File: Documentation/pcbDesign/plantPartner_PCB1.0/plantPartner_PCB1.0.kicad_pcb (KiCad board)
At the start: 2 copper layers, 148.3 x 67.3 mm, 86 parts, among them IC1 MPM3610, J1 Conn_01x04, J10 Screw_Terminal_01x03, J11 Conn_01x02, J12 Conn_01x03, J13 Conn_01x03, J14 Conn_01x03, J15 Conn_01x03, J16 Conn_01x04, J17 Conn_01x03, J18 Screw_Terminal_01x02, J19 Barrel_Jack, J2 Conn_01x04, J20 Conn_02x04_Top_Bottom, J21 Conn_01x04, J22 Conn_01x04, J23 Conn_01x01, J24 Conn_01x03, J25 Conn_01x03, J26 Conn_01x01, J27 Conn_01x01, J28 Conn_01x01, J29 Conn_01x02, J3 Conn_01x04, J30 Screw_Terminal_01x02, J4 Screw_Terminal, J5 Conn_01x02, J6 Screw_Terminal_01x03, J7 Conn_01x03, J8 Conn_02x04_Top_Bottom, J9 Conn_01x03, K1 SRD-05VDC-SL-C, K2 SRD-05VDC-SL-C, Q1 PNP, Q2 PNP, Q4 AO3400A, U1 EL357N-G, U2 MAX485, U3 ESP32-DEVKIT-V1, U4 EL357N-G

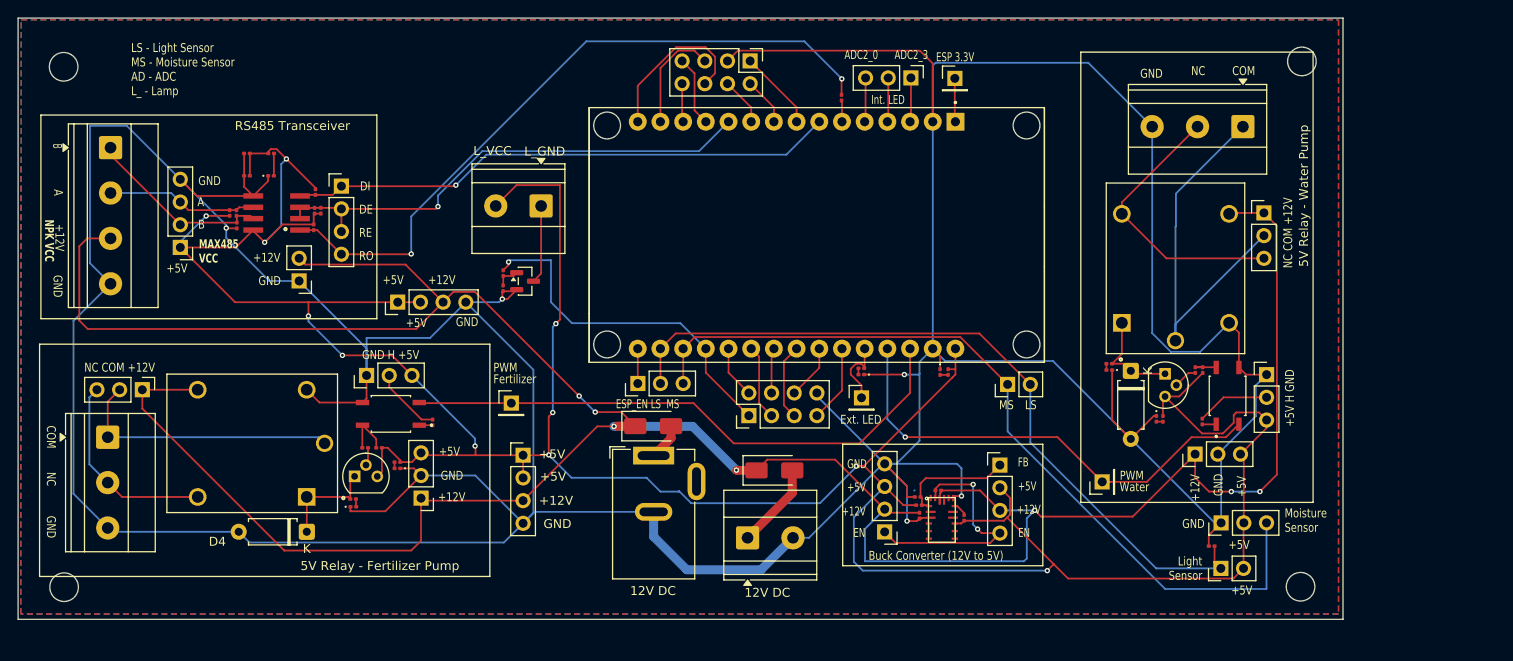
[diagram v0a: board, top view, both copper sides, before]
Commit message: Made some adjustments to PCB to fit JLCPCB standards. When going to order PCB realized I needed LCSC values. I spent the rest of the time trying to setup the JLCPCB tools plugin with zero success.
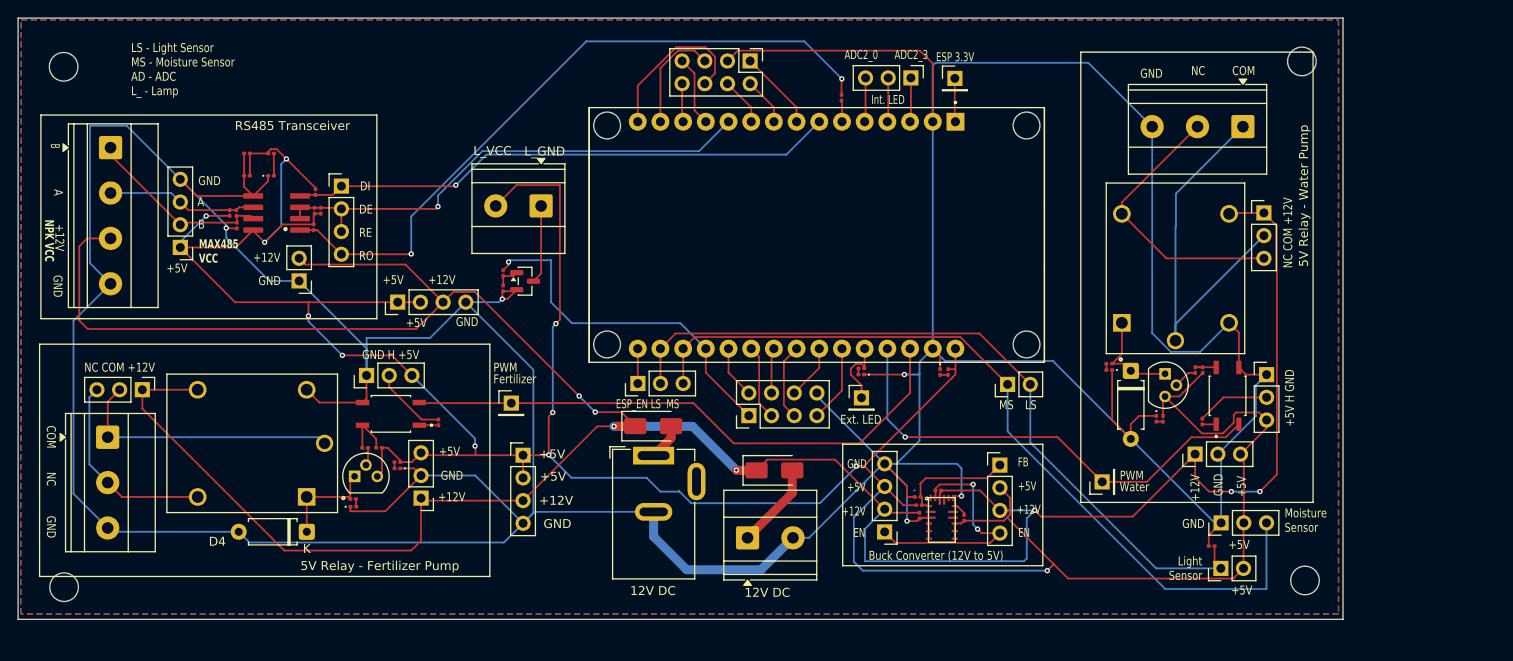
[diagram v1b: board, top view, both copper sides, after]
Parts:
- moved BottomRight 0.86 mm to (207.2, 114.2)
- moved R13 0.64 mm to (110.2, 96.6)
- renumbered REF** to BottomLeft, REF** to BottomRight, REF** to TopLeft, REF** to TopRight
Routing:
- net GND: track 579.2 -> 580.2 mm
- net Net-(R13-Pad2): track 1.54 -> 2.19 mm
- net /H: track 15.9 -> 16.5 mm
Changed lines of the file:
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@@
 		(tenting front back)
 		(pcbplotparams
-			(layerselection 0x00000000_00000000_55555555_575575ff)
+			(layerselection 0x00000000_00000000_55555555_5755f5ff)
 			(plot_on_all_layers_selection 0x00000000_00000000_00000000_00000000)
 			(disableapertmacros no)
@@
 			(usegerberattributes yes)
 			(usegerberadvancedattributes yes)
-			(creategerberjobfile yes)
+			(creategerberjobfile no)
 			(dashed_line_dash_ratio 12.000000)
 			(dashed_line_gap_ratio 3.000000)
@@
 			(sketchdnponfab yes)
 			(crossoutdnponfab yes)
-			(subtractmaskfromsilk yes)
+			(subtractmaskfromsilk no)
 			(outputformat 1)
 			(mirror no)
 			(drillshape 0)
 			(scaleselection 1)
-			(outputdirectory "")
+			(outputdirectory "GerberDrillFiles/")
 		)
 	)
@@
 	(footprint "Resistor_SMD:R_0201_0603Metric"
 		(layer "F.Cu")
-		(at 109.605 96.555 -90)
+		(at 110.25 96.555 -90)
 		(descr "Resistor SMD 0201 (0603 Metric), square (rectangular) end terminal, IPC-7351 nominal, (Body size source: https://www.vishay.com/docs/20052/crcw0201e3.pdf), generated with kicad-footprint-generator")
 		(tags "resistor")
@@
 		(descr "Mounting Hole 3.2mm, M3, no annular, generated by kicad-footprint-generator mountinghole.py")
 		(tags "mountinghole M3")
-		(property "Reference" "REF**"
+		(property "Reference" "TopLeft"
 			(at 0 -4.15 0)
 			(layer "F.SilkS")
@@
 		(descr "Mounting Hole 3.2mm, M3, no annular, generated by kicad-footprint-generator mountinghole.py")
 		(tags "mountinghole M3")
-		(property "Reference" "REF**"
+		(property "Reference" "TopRight"
 			(at 0 -4.15 0)
 			(layer "F.SilkS")
@@
 		(descr "Mounting Hole 3.2mm, M3, no annular, generated by kicad-footprint-generator mountinghole.py")
 		(tags "mountinghole M3")
-		(property "Reference" "REF**"
+		(property "Reference" "BottomLeft"
 			(at 0 -4.15 0)
 			(layer "F.SilkS")
@@
 		(tags "resistor")
 		(property "Reference" "R10"
-			(at 1.765 -0.2388 90)
+			(at 1.765 -0.6388 90)
 			(layer "B.SilkS")
 			(effects
@@
 	(footprint "MountingHole:MountingHole_3.2mm_M3"
 		(layer "F.Cu")
-		(at 206.75 114.95)
+		(at 207.25 114.25)
 		(descr "Mounting Hole 3.2mm, M3, no annular, generated by kicad-footprint-generator mountinghole.py")
 		(tags "mountinghole M3")
-		(property "Reference" "REF**"
+		(property "Reference" "BottomRight"
 			(at 0 -4.15 0)
 			(layer "F.SilkS")
@@
 		(fp_text user "K"
 			(at 0 -1.9 90)
-			(layer "F.SilkS")
-			(effects
-				(font
-					(size 1 1)
-					(thickness 0.15)
-				)
-			)
-		)
-		(fp_text user "K"
-			(at 0 -1.9 90)
 			(layer "F.Fab")
 			(effects
@@
 	)
 	(gr_text "B"
-		(at 67 65.35 270)
+		(at 66.75 65.35 270)
 		(layer "F.SilkS")
 		(effects
@@
 	)
 	(segment
+		(start 188.67 95.83)
+		(end 187.75 96.75)
+		(width 0.2)
+		(layer "F.Cu")
+		(net 1)
+	)
+	(segment
 		(start 81.355 69.35)
 		(end 83.215 71.21)
@@
 	)
 	(segment
-		(start 190.324999 95.83)
-		(end 187.75 98.404999)
-		(width 0.2)
-		(layer "F.Cu")
-		(net 1)
-	)
-	(segment
 		(start 87.47 108.375)
 		(end 87.895 108.8)
@@
 	)
 	(segment
-		(start 83.215 71.21)
-		(end 89.5226 71.21)
+		(start 187.75 96.75)
+		(end 187.75 98.404999)
 		(width 0.2)
 		(layer "F.Cu")
@@
 	(segment
 		(start 190.61 95.83)
-		(end 190.324999 95.83)
+		(end 188.67 95.83)
+		(width 0.2)
+		(layer "F.Cu")
+		(net 1)
+	)
+	(segment
+		(start 83.215 71.21)
+		(end 89.5226 71.21)
 		(width 0.2)
 		(layer "F.Cu")
@@
 	)
 	(segment
+		(start 110.25 96.875)
+		(end 109.605 96.875)
+		(width 0.2)
+		(layer "F.Cu")
+		(net 10)
+	)
+	(segment
 		(start 108.138 96.9)
 		(end 108.108 96.87)
@@
 	)
 	(segment
-		(start 104.745 91.3)
+		(start 108.361 96.235)
 		(end 104.745 92.619)
 		(width 0.2)
@@
 	)
 	(segment
-		(start 108.361 96.235)
-		(end 109.605 96.235)
+		(start 198.135 93.75)
+		(end 195.75 96.135)
 		(width 0.2)
 		(layer "F.Cu")
@@
 	)
 	(segment
-		(start 198.135 93.75)
-		(end 195.75 96.135)
+		(start 202.95 93.75)
+		(end 198.135 93.75)
 		(width 0.2)
 		(layer "F.Cu")
@@
 	(segment
 		(start 104.745 92.619)
-		(end 108.361 96.235)
+		(end 104.745 91.3)
 		(width 0.2)
 		(layer "F.Cu")
@@
 	)
 	(segment
-		(start 202.95 93.75)
-		(end 198.135 93.75)
+		(start 110.25 96.235)
+		(end 108.361 96.235)
 		(width 0.2)
 		(layer "F.Cu")

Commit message: I got the plugin finally working! I had some messed up Python modules that I had to remove and then reinstall. I have also now learned that the footprints I chose for the PCB were too small and classified as extended for JLCPCB which means more 4189. So now I have to change all the Resistor, Capacitor, and Diode footprints to a bigger size to not cost too much. This will then also result in me having to route these small parts again. I am tired of my lack of PCB design knowledge but I think I might be done after this.
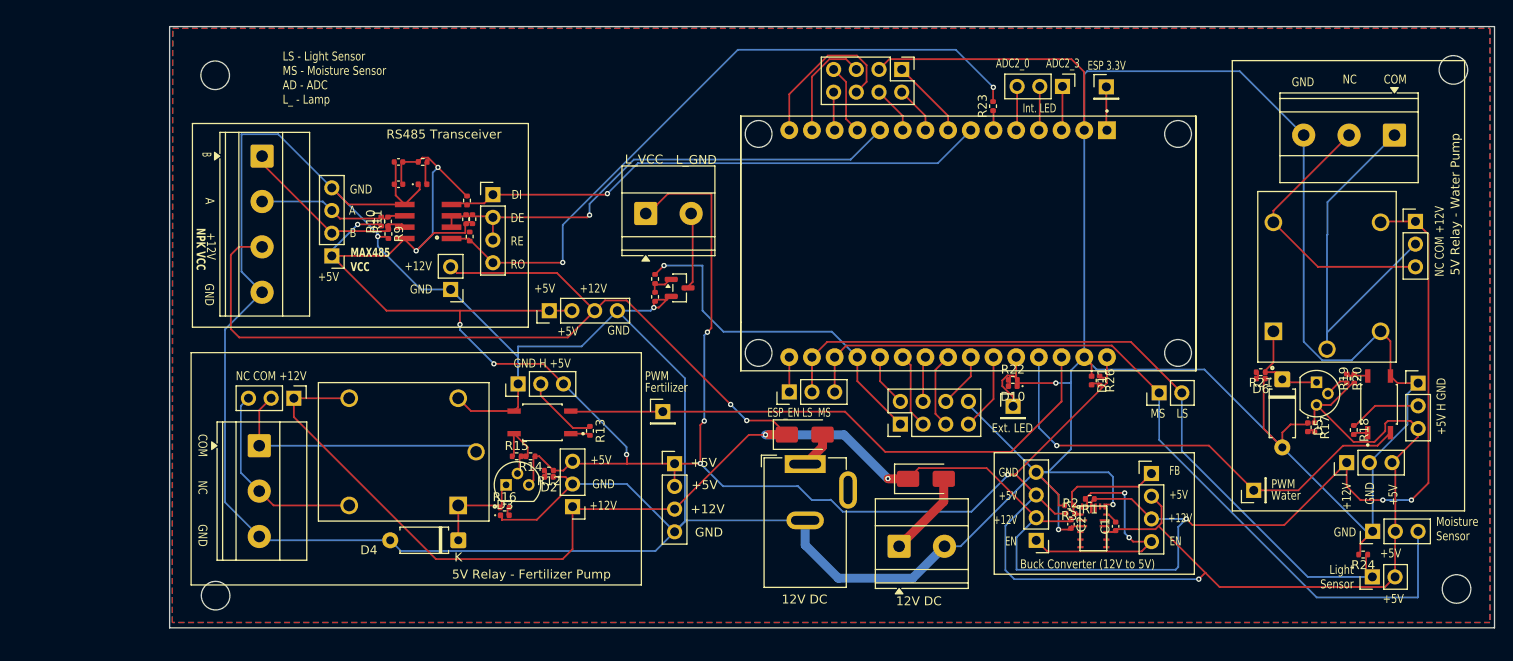
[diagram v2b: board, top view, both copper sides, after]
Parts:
- C1, C2, C3, C4: footprint Capacitor_SMD:C_0201_0603Metric -> Capacitor_SMD:C_0402_1005Metric
- D1, D10, D11, D2, D3, D5, D6: footprint LED_SMD:LED_0201_0603Metric -> LED_SMD:LED_0402_1005Metric
- R1, R10, R11, R12, R13, R14, R15, R16, R17, R18, R19, R2, R20, R21, R22, R23, R24, R25, R26, R27, R3, R4, R5, R6, R7, R8, R9: footprint Resistor_SMD:R_0201_0603Metric -> Resistor_SMD:R_0402_1005Metric
- moved R4 17.5 mm to (113.8, 75.8)
- moved Q4 17.3 mm to (137.2, 81.5)
- moved R27 17.0 mm to (134.5, 82.5)
- moved R25 17.0 mm to (134.5, 80.5)
- moved D10 17.0 mm to (174.5, 92.5)
- moved R22 17.0 mm to (174.5, 91.8)
- moved BottomLeft 17.0 mm to (85.3, 116.0)
- moved BottomRight 17.0 mm to (224.2, 115.2)
- moved C1 17.0 mm to (186.1, 108.2)
- moved C2 17.0 mm to (181.1, 107.9)
- moved C3 17.0 mm to (105.8, 69.9)
- moved C4 17.0 mm to (105.8, 67.4)
- moved D11 17.0 mm to (183.4, 91.9)
- moved D2 17.0 mm to (122.6, 102.7)
- moved D3 17.0 mm to (117.7, 107.0)
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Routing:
- net +5V: track 352.4 -> 361.1 mm
- net /Drain: track 8.78 -> 0.00 mm

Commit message: Rerouted the resistors, capacitors, and LEDs. Surely I can now generate the Drill & Gerber files for printing with no issues
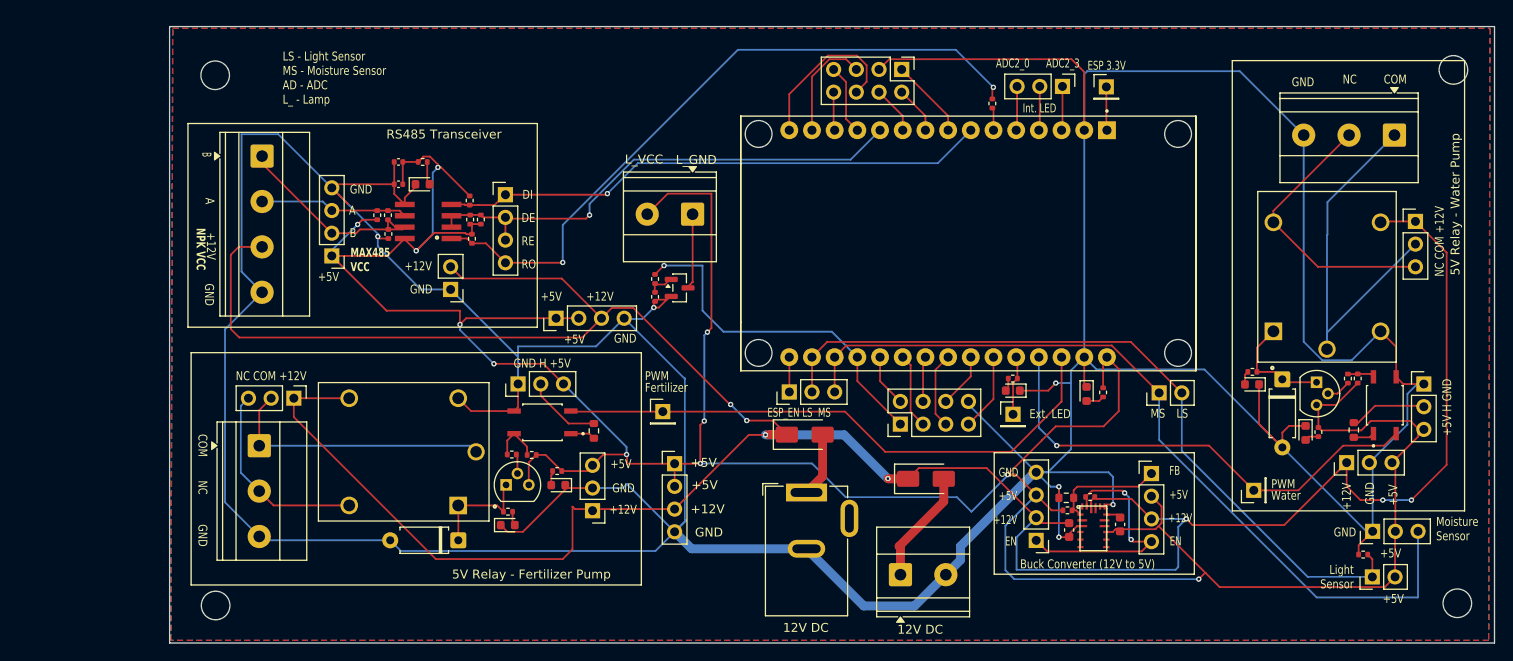
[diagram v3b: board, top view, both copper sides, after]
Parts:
- C1, C2: footprint Capacitor_SMD:C_0402_1005Metric -> Capacitor_SMD:C_0603_1608Metric
- D1, D10, D11, D2, D3, D5, D6: footprint LED_SMD:LED_0402_1005Metric -> LED_SMD:LED_0603_1608Metric
- R13, R18, R3: footprint Resistor_SMD:R_0402_1005Metric -> Resistor_SMD:R_0603_1608Metric
- moved J30 5.25 mm to (138.7, 73.2), turned to 180 degrees
- moved J19 3.18 mm to (151.4, 104.4)
- moved J18 3.18 mm to (162.0, 113.6)
- moved J14 2.28 mm to (127.5, 106.4)
- moved D11 1.60 mm to (182.8, 93.4)
- moved BottomRight 1.60 mm to (224.3, 116.8)
- moved J2 1.40 mm to (117.8, 71.1)
- moved D2 1.40 mm to (123.7, 103.6)
- moved R26 1.39 mm to (184.7, 93.2)
- moved D6 1.18 mm to (201.3, 92.3)
- moved D3 1.15 mm to (118.0, 108.0)
- moved J21 1.14 mm to (123.4, 84.9)
- moved BottomLeft 1.10 mm to (85.3, 117.0)
- moved R5 0.95 mm to (115.0, 73.8)
- moved R21 0.94 mm to (201.4, 90.9)
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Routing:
- net /Drain: track 0.00 -> 8.81 mm
- net /12V_JACK: track 4.11 -> 9.52 mm
- net /12V_SCREW: track 9.62 -> 12.9 mm
- net /B: track 21.1 -> 24.0 mm
- net +12V: track 331.7 -> 333.9 mm
- net GND: track 580.2 -> 578.5 mm, vias 5 -> 6
- net Net-(D4-K): track 11.6 -> 13.1 mm
- net +5V: track 361.1 -> 359.7 mm
- net /EXTERNAL LED: track 8.02 -> 6.65 mm
- net Net-(D11-A): track 0.90 -> 2.04 mm
- net Net-(D7-K): track 11.9 -> 12.9 mm
- net Net-(D2-A): track 0.71 -> 1.64 mm
- net /ADC_LIGHT_SENSOR: track 84.8 -> 85.7 mm
- net Net-(D5-A): track 0.74 -> 1.59 mm
- net Net-(D6-A): track 0.71 -> 1.53 mm
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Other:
- board size 148.3 x 67.3 mm -> 148.3 x 69 mm
- board text removed: "C1"
- board text removed: "C2"
- board text removed: "D1"
- board text removed: "D10"
- board text removed: "D11"
- board text removed: "D4"
- board text removed: "D5"
- board text removed: "D6"
- board text removed: "R1"
- board text removed: "R17"
- board text removed: "R18"
- board text removed: "R19"
- board text removed: "R2"
- board text removed: "R20"
- board text removed: "R21"
- board text removed: "R22"
- board text removed: "R23"
- board text removed: "R24"
- board text removed: "R26"
- board text removed: "R3"

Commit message: I ordered the PCBgit add . … there is so many changes I want to make but I also just wanted to order it but without the revisions it was more expensive but now we at least will have a board. Welp, either way I will solve the NPK (again unfortunately) next and then after that get onto PCB V2 and then 3D modeling
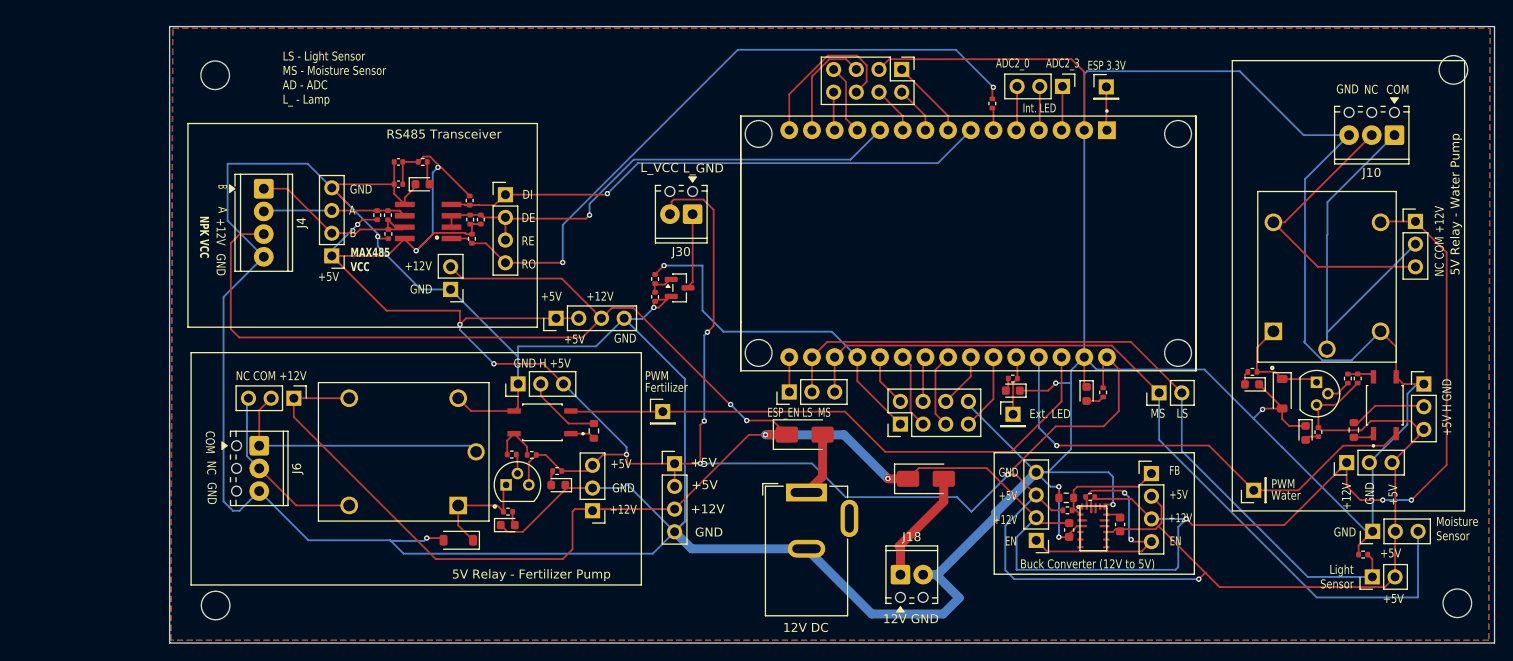
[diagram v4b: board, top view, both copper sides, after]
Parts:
- D4, D7: value 1N400x -> 1N4148W; footprint Diode_THT:D_A-405_P7.62mm_Horizontal -> Diode_SMD:D_SOD-123
- J10, J6: footprint TerminalBlock_Phoenix:TerminalBlock_Phoenix_MKDS-1,5-3-5.08_1x03_P5.08mm_Horizontal -> TerminalBlock_Phoenix:TerminalBlock_Phoenix_MPT-0,5-3-2.54_1x03_P2.54mm_Horizontal
- J18, J30: footprint TerminalBlock_Phoenix:TerminalBlock_Phoenix_MKDS-1,5-2-5.08_1x02_P5.08mm_Horizontal -> TerminalBlock_Phoenix:TerminalBlock_Phoenix_MPT-0,5-2-2.54_1x02_P2.54mm_Horizontal
- J4: footprint TerminalBlock_Phoenix:TerminalBlock_Phoenix_MKDS-1,5-4-5.08_1x04_P5.08mm_Horizontal -> TerminalBlock_Phoenix:TerminalBlock_Phoenix_MPT-0,5-4-2.54_1x04_P2.54mm_Horizontal
- moved J4 3.65 mm to (90.7, 70.4)
- moved D7 1.62 mm to (204.7, 93.3)
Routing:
- net GND: track 578.5 -> 598.6 mm, vias 6 -> 8
- net +5V: track 359.7 -> 356.6 mm
- net /B: track 24.0 -> 21.8 mm
- net +12V: track 333.9 -> 334.9 mm
- net Net-(D4-K): track 13.1 -> 13.8 mm
- net /A: track 16.6 -> 16.1 mm
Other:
- board text added: "12V GND"
- board text removed: "D7"
